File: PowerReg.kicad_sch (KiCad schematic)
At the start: 24 parts, among them Q12 DMP3099L, Q13 DMP3099L

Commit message: Lots of cleanup and updates; Waiting on PR approval for GPS filter
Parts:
- renumbered C43 to C51, C44 to C52, C45 to C53, C46 to C54, D24 to D26, D25 to D27, D26 to D28, D27 to D29, D28 to D30, U26 to U29, U27 to U30, U28 to U31, U29 to U32

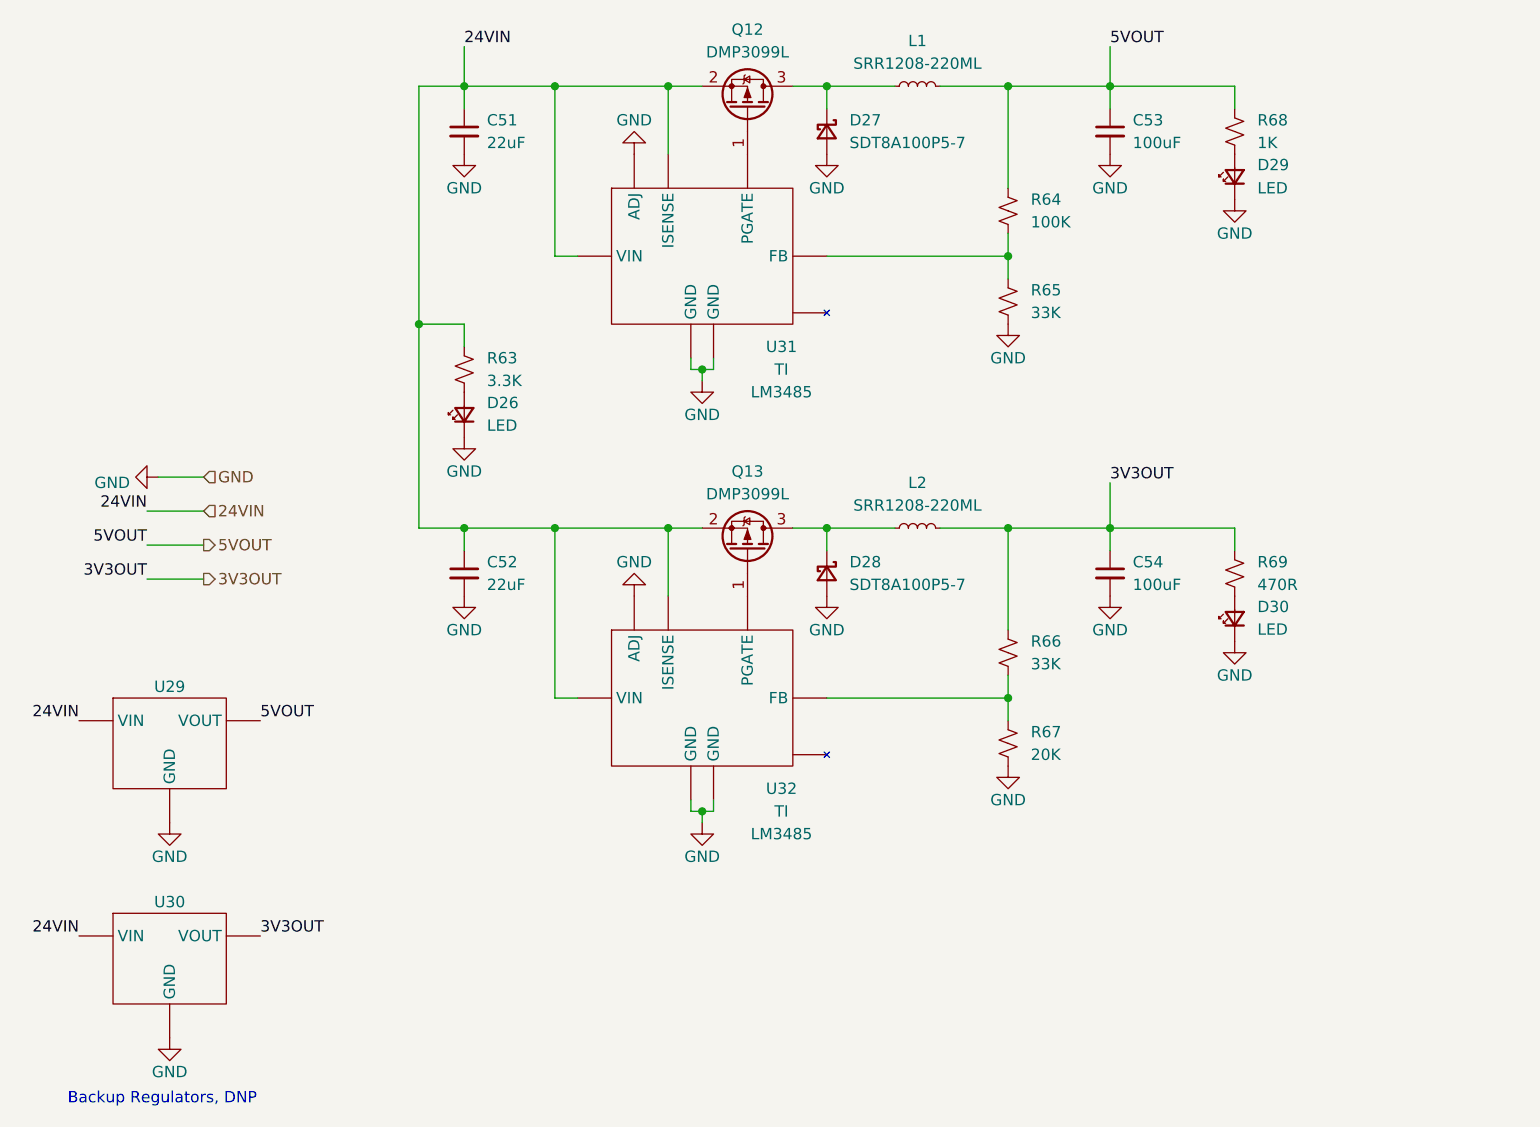
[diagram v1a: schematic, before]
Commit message: Updated so only STM pins left really
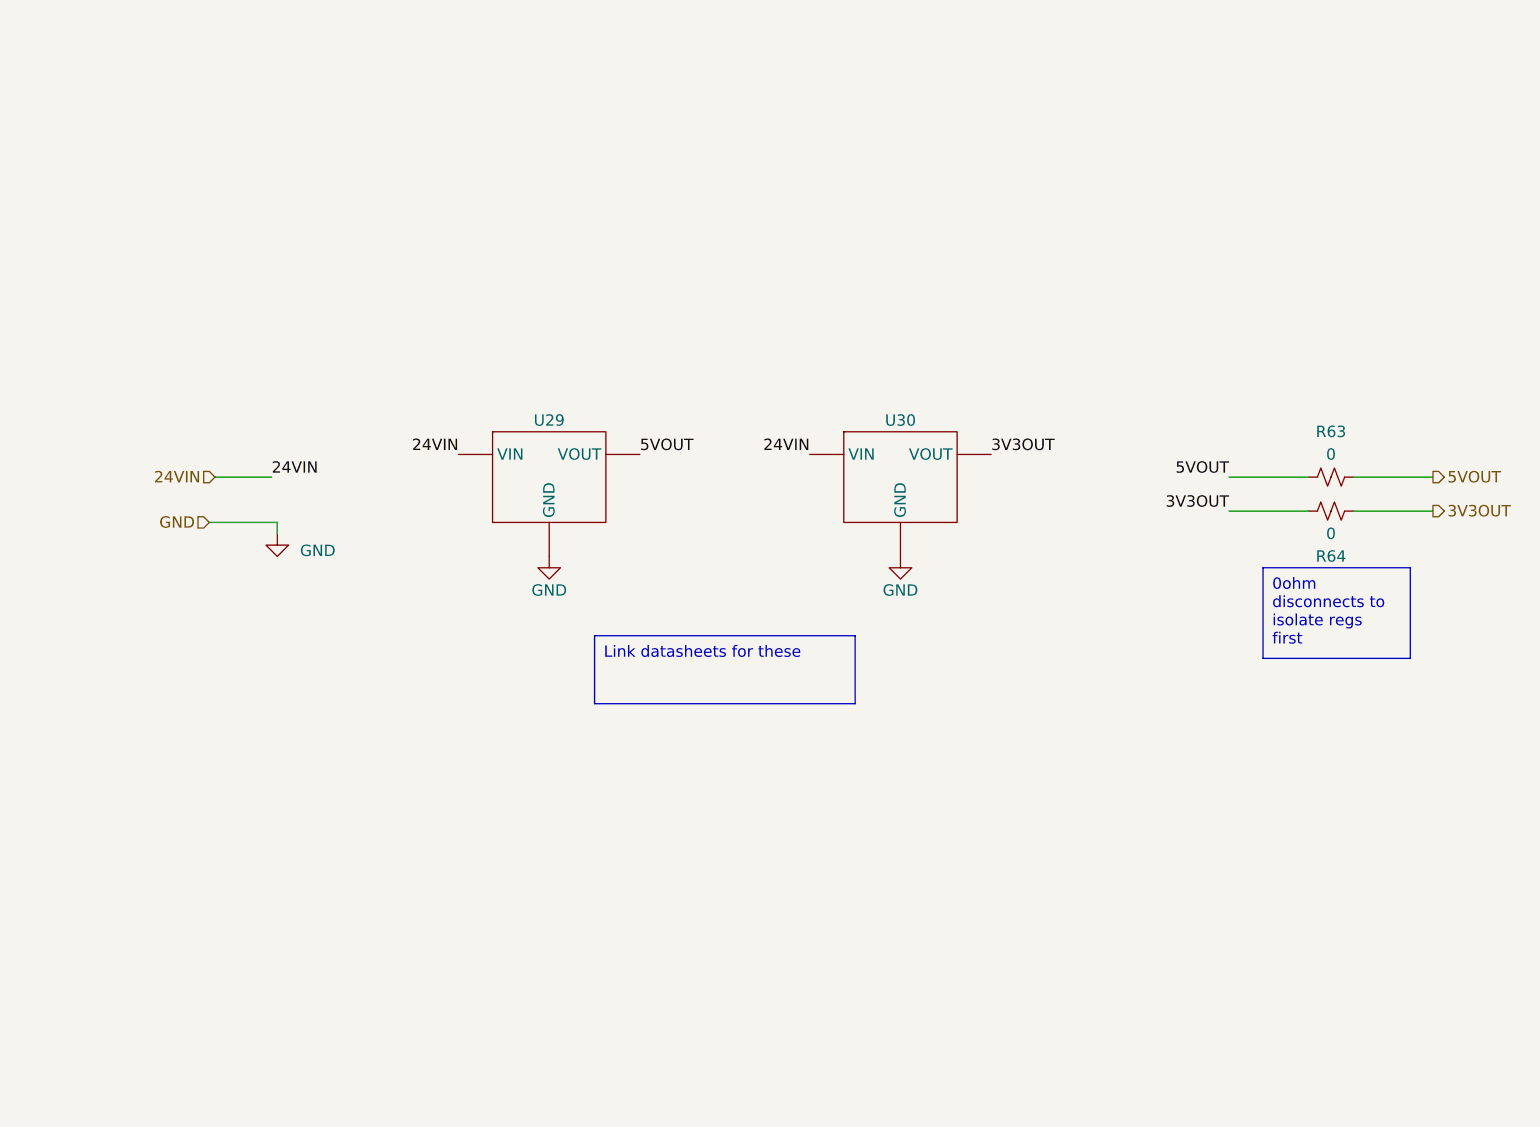
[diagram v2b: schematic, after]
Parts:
- removed C51, C52: 22uF, Capacitor_SMD:C_1206_3216Metric, symbol Device:C_Small
- removed C53, C54: 100uF, Capacitor_SMD:C_1206_3216Metric, symbol Device:C_Small
- removed D26, D29, D30: LED, LED_SMD:LED_0603_1608Metric, symbol Device:LED_Small
- removed D27, D28: SDT8A100P5-7, Diode_SMD:D_PowerDI-5, symbol Device:D_Schottky_Small
- removed L1, L2: SRR1208-220ML, Inductor_SMD:L_Bourns_SRR1208_12.7x12.7mm, symbol Device:L_Small
- removed Q12, Q13: DMP3099L, Package_TO_SOT_SMD:SOT-23-3, symbol Device:Q_PMOS_GSD
- removed R65, R66: 33K, Resistor_SMD:R_0402_1005Metric, symbol Device:R_Small_US
- removed R67: 20K, Resistor_SMD:R_0402_1005Metric, symbol Device:R_Small_US
- removed R68: 1K, Resistor_SMD:R_0402_1005Metric, symbol Device:R_Small_US
- removed R69: 470R, Resistor_SMD:R_0402_1005Metric, symbol Device:R_Small_US
- removed U31, U32: ~, Package_SO:VSSOP-8_3.0x3.0mm_P0.65mm, symbol UCIRP-KiCAD-Lib:LM3485
- R63: value 3.3K -> 0; footprint Resistor_SMD:R_0402_1005Metric -> Resistor_SMD:R_1206_3216Metric_Pad1.30x1.75mm_HandSolder; Manufacturer Generic -> (none); Part # Generic 3.3K 1% 0402 Resistor -> (none)
- R64: value 100K -> 0; footprint Resistor_SMD:R_0402_1005Metric -> Resistor_SMD:R_1206_3216Metric_Pad1.30x1.75mm_HandSolder; Manufacturer Generic -> (none); Part # Generic 100K 1% 0402 Resistor -> (none)
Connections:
- net 24VIN: no longer R63.2
- net 3V3OUT: now also R64.1, R64.2
- net 5VOUT: now also R63.1, R63.2; no longer R64.2
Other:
- note removed: "Backup Regulators, DNP"
- moved on the sheet: U29, U30

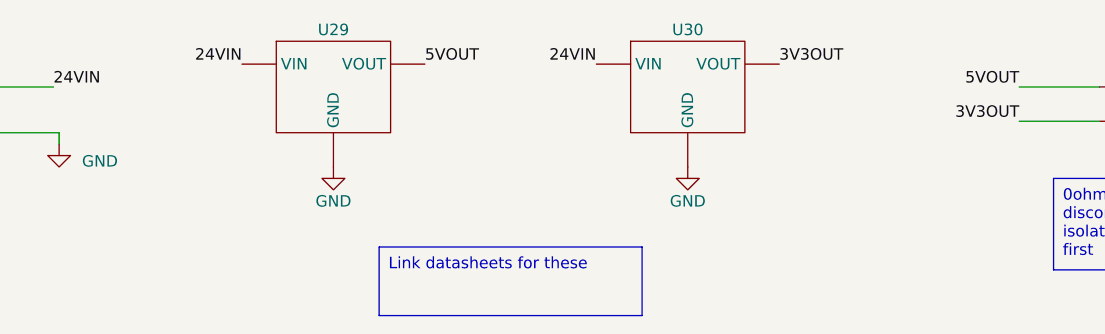
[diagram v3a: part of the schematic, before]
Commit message: added flash memory and ldos
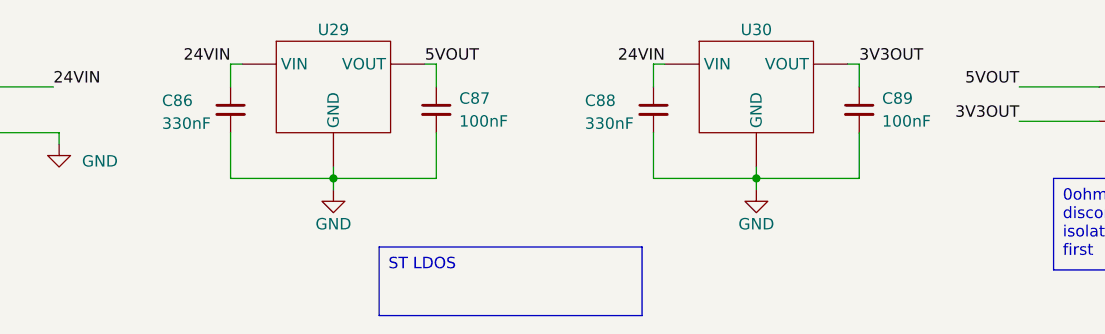
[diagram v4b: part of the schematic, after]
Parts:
- added C86, C88: 330nF, Capacitor_SMD:C_0603_1608Metric, symbol Device:C_Small
- added C87, C89: 100nF, Capacitor_SMD:C_0603_1608Metric, symbol Device:C_Small
- U29: footprint Package_TO_SOT_THT:TO-220-3_Vertical -> Package_SO:SOIC-8_3.9x4.9mm_P1.27mm; Manufacturer (none) -> STMicroelectronics; Part # (none) -> L78L05ACD13TR
- U30: footprint Package_TO_SOT_THT:TO-220-3_Vertical -> Package_TO_SOT_SMD:SOT-89-3; Manufacturer (none) -> STMicroelectronics; Part # (none) -> L78L33ABUTR
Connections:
- net 24VIN: now also C86.1, C88.1
- net 3V3OUT: now also C89.1
- net 5VOUT: now also C87.1
- net GND: now also C86.2, C87.2, C88.2, C89.2
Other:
- moved on the sheet: U30

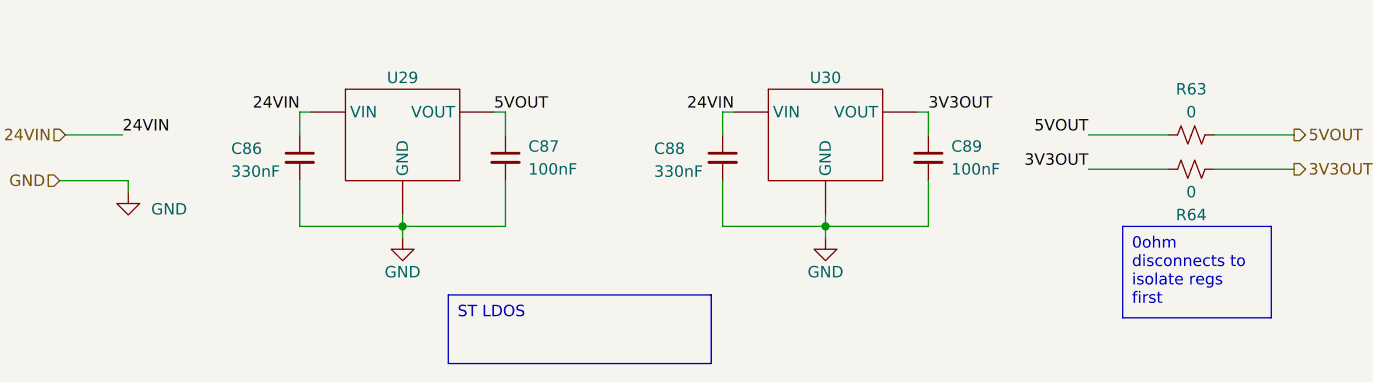
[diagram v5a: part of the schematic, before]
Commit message: 8.02 Update; Also changed VRMs and added some notes
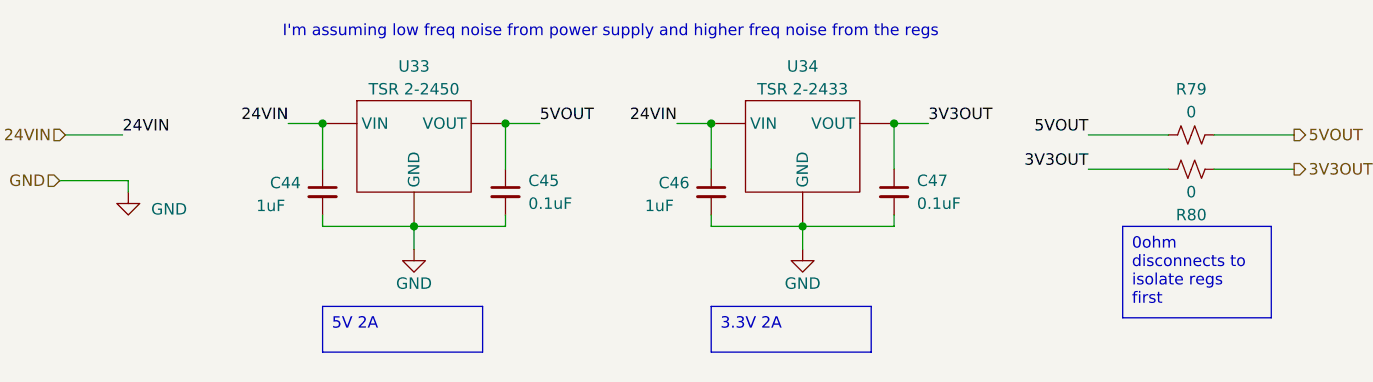
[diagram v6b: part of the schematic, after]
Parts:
- removed C86, C88: 330nF, Capacitor_SMD:C_0603_1608Metric, symbol Device:C_Small
- removed C87, C89: 100nF, Capacitor_SMD:C_0603_1608Metric, symbol Device:C_Small
- removed U29: ~, Package_SO:SOIC-8_3.9x4.9mm_P1.27mm, symbol UCIRP-KiCAD-Lib:Generic_Regulator_InputGroundOutput
- removed U30: ~, Package_TO_SOT_SMD:SOT-89-3, symbol UCIRP-KiCAD-Lib:Generic_Regulator_InputGroundOutput
- added C44, C46: 1uF, symbol Device:C_Small
- added C45, C47: 0.1uF, symbol Device:C_Small
- added U33, U34: ~, symbol UCIRP-KiCAD-Lib:Generic_Regulator_InputGroundOutput
- renumbered R63 to R79, R64 to R80
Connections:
- net 24VIN: now also C44.1, C46.1, U33.1 (VIN), U34.1 (VIN)
- net 3V3OUT: now also C47.1, U34.3 (VOUT)
- net 5VOUT: now also C45.1, U33.3 (VOUT)
- net GND: now also C44.2, C45.2, C46.2, C47.2, U33.2 (GND), U34.2 (GND)
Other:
- note added: "I'm assuming low freq noise from power supply and higher freq noise from the regs"

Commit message: ECU essentially reviewable
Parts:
- renumbered R79 to R84, R80 to R85, U33 to U32, U34 to U33
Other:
- note added: "Should I also use the same regs in REDS here?"
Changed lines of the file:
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@@
+		)
+	)
+	(text "Should I also use the same regs in REDS here?"
+		(exclude_from_sim no)
+		(at 164.846 69.342 0)
+		(effects
+			(font
+				(size 1.27 1.27)
+				(color 255 0 4 1)
+			)
 		)
 	)
@@
 		(on_board yes)
 		(dnp no)
-		(property "Reference" "#PWR0135"
+		(property "Reference" "#PWR0133"
 			(at 182.88 110.49 0)
 			(effects
@@
 			(project "rocket2-ecu"
 				(path "/02606b2c-b376-4ffb-9781-f9cea3f70994/944e98dc-4249-4ad7-a352-e05a5cc42499"
-					(reference "#PWR0135")
+					(reference "#PWR0133")
 					(unit 1)
 				)
@@
 		(on_board yes)
 		(dnp no)
-		(property "Reference" "R80"
+		(property "Reference" "R85"
 			(at 226.06 100.33 90)
 			(effects
@@
 			(project "rocket2-ecu"
 				(path "/02606b2c-b376-4ffb-9781-f9cea3f70994/944e98dc-4249-4ad7-a352-e05a5cc42499"
-					(reference "R80")
+					(reference "R85")
 					(unit 1)
 				)
@@
 		(dnp no)
 		(fields_autoplaced yes)
-		(property "Reference" "#PWR0133"
+		(property "Reference" "#PWR0131"
 			(at 107.95 104.14 0)
 			(effects
@@
 			(project "rocket2-ecu"
 				(path "/02606b2c-b376-4ffb-9781-f9cea3f70994/944e98dc-4249-4ad7-a352-e05a5cc42499"
-					(reference "#PWR0133")
+					(reference "#PWR0131")
 					(unit 1)
 				)
@@
 		(dnp no)
 		(fields_autoplaced yes)
-		(property "Reference" "R79"
+		(property "Reference" "R84"
 			(at 226.06 86.36 90)
 			(effects
@@
 			(project "rocket2-ecu"
 				(path "/02606b2c-b376-4ffb-9781-f9cea3f70994/944e98dc-4249-4ad7-a352-e05a5cc42499"
-					(reference "R79")
+					(reference "R84")
 					(unit 1)
 				)
@@
 		(on_board yes)
 		(dnp no)
-		(property "Reference" "U33"
+		(property "Reference" "U32"
 			(at 139.7 83.82 0)
 			(effects
@@
 			(project "rocket2-ecu"
 				(path "/02606b2c-b376-4ffb-9781-f9cea3f70994/944e98dc-4249-4ad7-a352-e05a5cc42499"
-					(reference "U33")
+					(reference "U32")
 					(unit 1)
 				)
@@
 		(on_board yes)
 		(dnp no)
-		(property "Reference" "U34"
+		(property "Reference" "U33"
 			(at 182.88 83.82 0)
 			(effects
@@
 			(project "rocket2-ecu"
 				(path "/02606b2c-b376-4ffb-9781-f9cea3f70994/944e98dc-4249-4ad7-a352-e05a5cc42499"
-					(reference "U34")
+					(reference "U33")
 					(unit 1)
 				)
@@
 		(on_board yes)
 		(dnp no)
-		(property "Reference" "#PWR0134"
+		(property "Reference" "#PWR0132"
 			(at 139.7 110.49 0)
 			(effects
@@
 			(project "rocket2-ecu"
 				(path "/02606b2c-b376-4ffb-9781-f9cea3f70994/944e98dc-4249-4ad7-a352-e05a5cc42499"
-					(reference "#PWR0134")
-					(unit 1)
-				)
+					(reference "#PWR0132")
+					(unit 1)
+				)
